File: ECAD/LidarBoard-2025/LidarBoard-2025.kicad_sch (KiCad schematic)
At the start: 17 parts, among them J1 Serial_Strategy, J2 Serial_Lidar, J3 Conn_01x03, J4 Oled, U1 Teensy3.2, U2 AMS1117-3.3

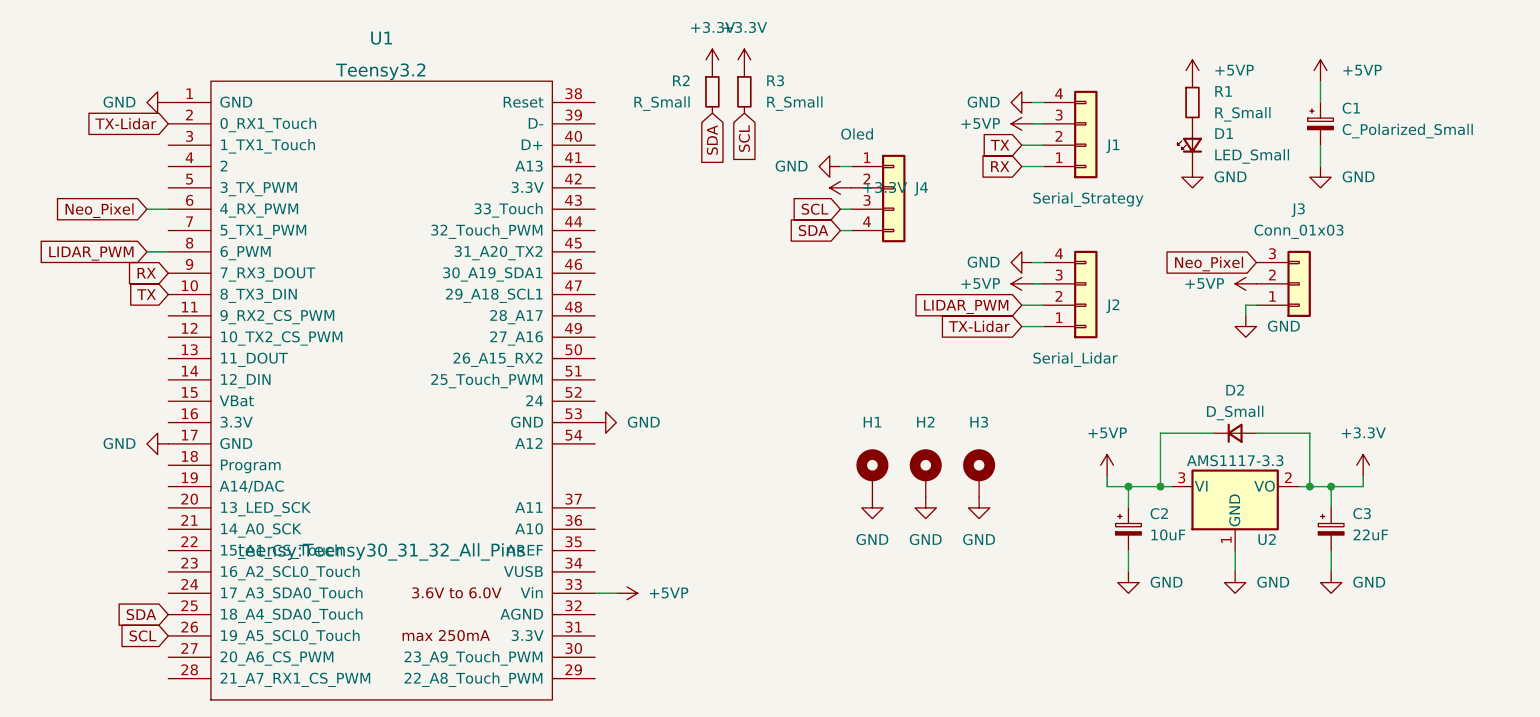
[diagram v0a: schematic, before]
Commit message: switch to KiCad 8 - Create Localisation version
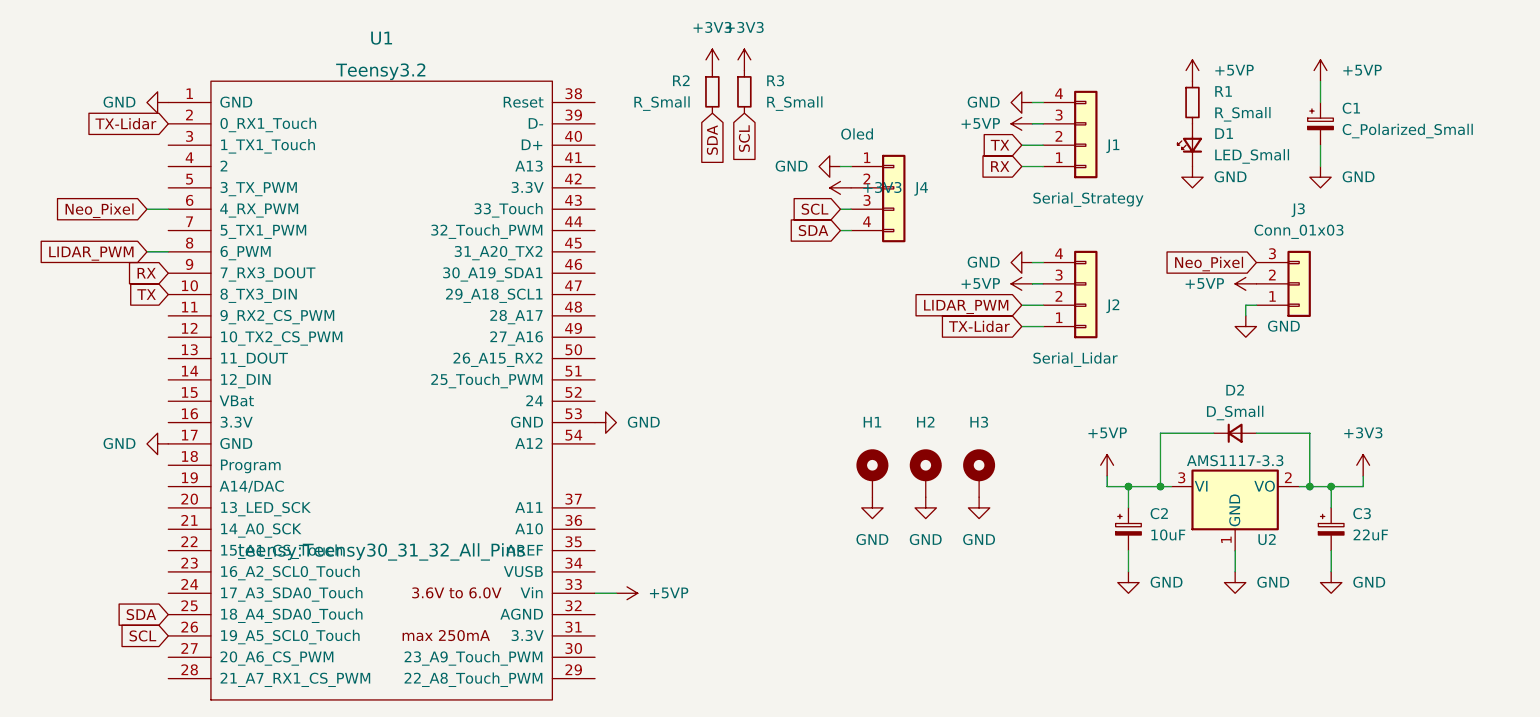
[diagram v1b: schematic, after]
